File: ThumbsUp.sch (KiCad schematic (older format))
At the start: 169 parts, among them IC1 RP2040, IC2 W25Q128JVSIM, IC3 RP2040, IC4 W25Q128JVSIM, J1 Conn_01x04_Male, J10 Raiser_Male, J11 Raiser_Female, J12 Raiser_Male, J13 Raiser_Female, J14 Raiser_Male, J15 Raiser_Female, J16 Raiser_Male, J17 Raiser_Female, J18 Raiser_Male, J19 Raiser_Female, J2 Conn_01x04_Male, J20 Conn_01x04_Female, J21 Conn_01x04_Female, J22 Conn_01x04_Female, J23 Conn_01x04_Female, J24 Conn_01x04_Male, J25 Conn_01x04_Male, J26 Conn_01x04_Male, J27 Conn_01x04_Male, J28 Conn_01x04_Female, J29 Conn_01x04_Female, J3 Conn_01x04_Female, J30 Conn_01x04_Female, J31 Conn_01x04_Female, J32 USB_C_Receptacle_USB2.0, J33 Raiser_Male, J34 Raiser_Female, J35 Raiser_Male, J36 STX-3501-3N, J37 USB_C_Receptacle_USB2.0, J38 Raiser_Female, J39 Raiser_Male, J4 Conn_01x04_Male, J40 Raiser_Female, J41 Raiser_Male, J42 Raiser_Female, J43 Raiser_Male, J44 Raiser_Female, J45 Raiser_Male, J46 STX-3501-3N, J47 Raiser_Female, J48 Raiser_Male, J49 Raiser_Female, J5 Conn_01x04_Female, J50 Raiser_Male, J51 Raiser_Female, J52 Raiser_Male, J6 Conn_01x04_Male, J7 Conn_01x04_Male, J8 Conn_01x04_Male, J9 Raiser_Female, U1 NCP1117-3.3_SOT223, U2 NCP1117-3.3_SOT223, Y1 ABLS-12.000MHZ-B4-T, Y2 ABLS-12.000MHZ-B4-T

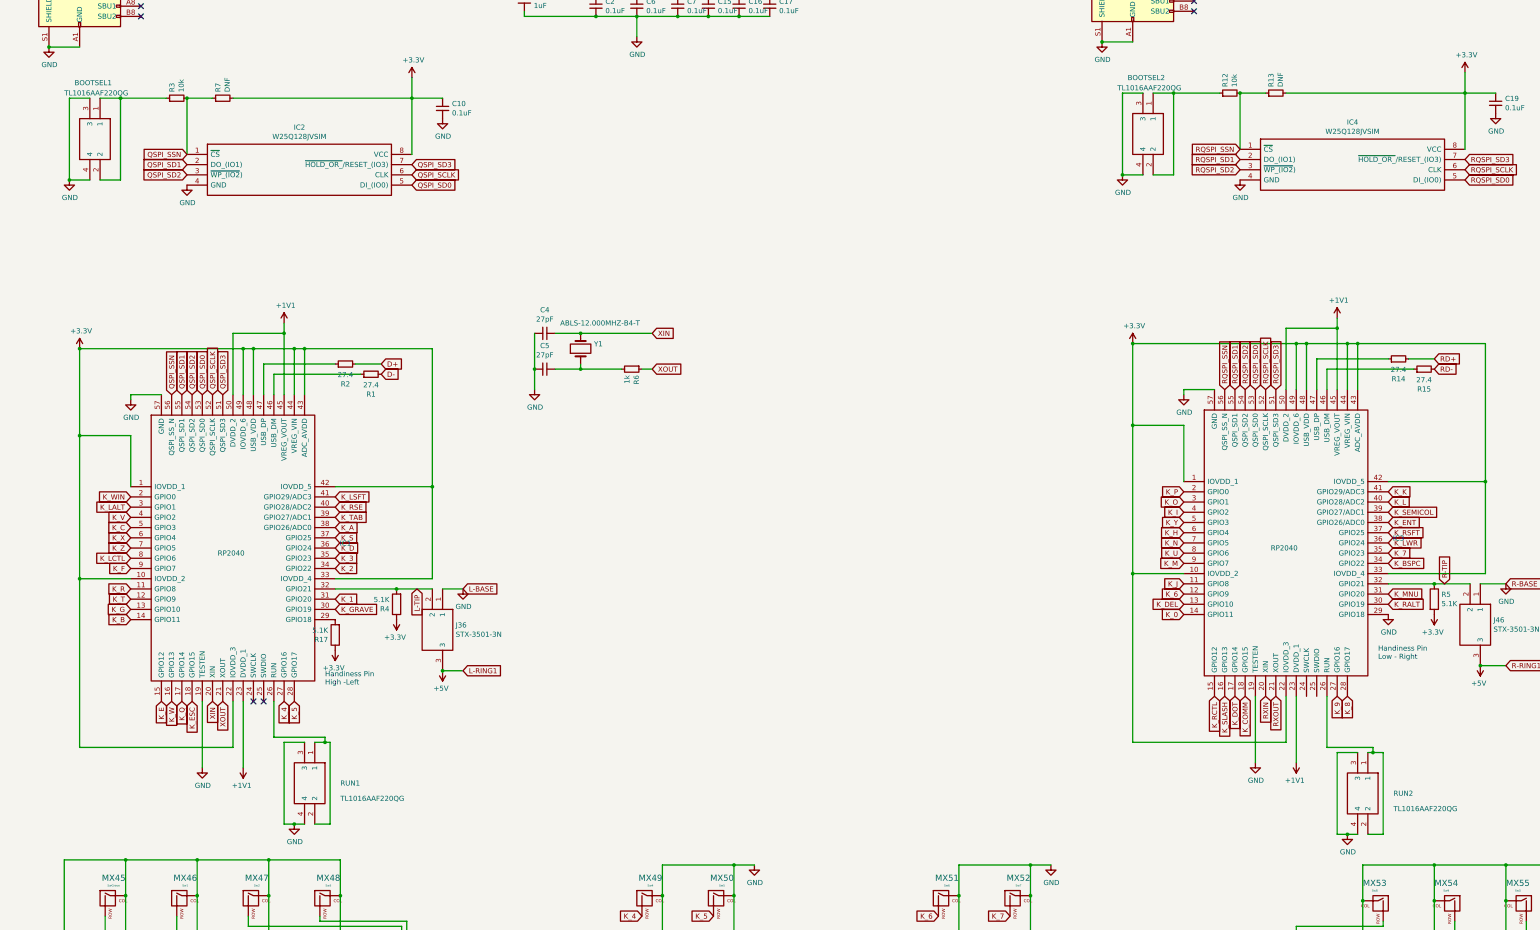
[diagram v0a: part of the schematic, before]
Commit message: Adjusted outlines, replaced pushbuttons
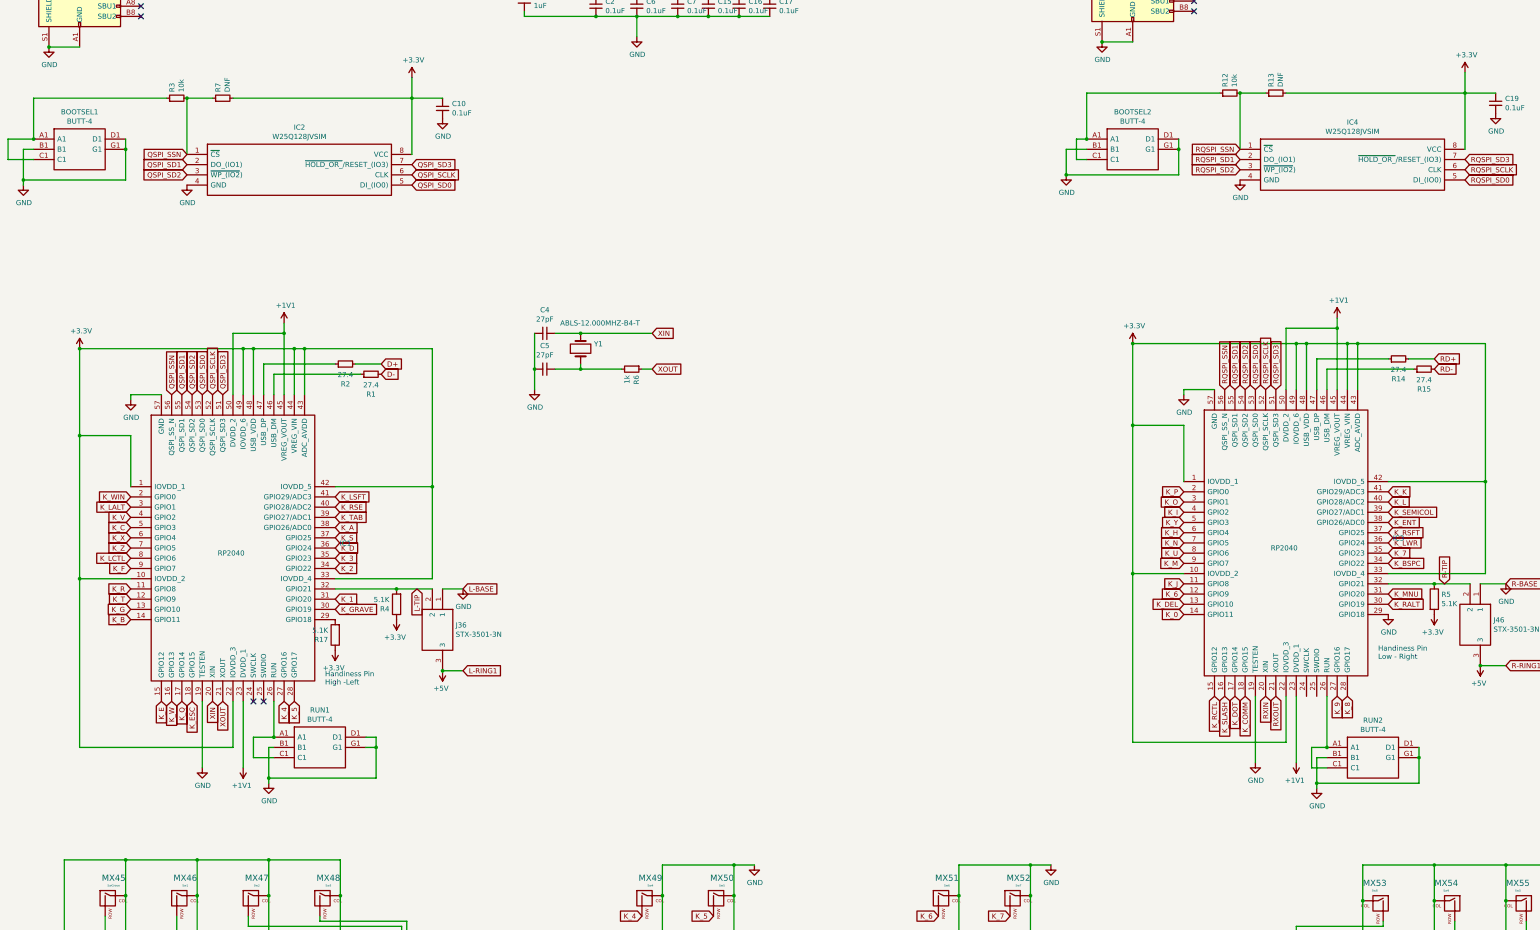
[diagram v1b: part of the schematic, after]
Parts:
- removed BOOTSEL1, BOOTSEL2, RUN1, RUN2: TL1016AAF220QG, TL1016AAF220QG:TL1016AAF220QG, symbol TL1016AAF220QG:TL1016AAF220QG
- added BOOTSEL1, BOOTSEL2, RUN1, RUN2: BUTT-4, BUTT4, symbol BUTT-4:BUTT-4
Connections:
- net GND: now also BOOTSEL1.B1, BOOTSEL1.D1, BOOTSEL1.G1, BOOTSEL2.B1, BOOTSEL2.D1, BOOTSEL2.G1, RUN1.B1, RUN1.D1, RUN1.G1, RUN2.B1, RUN2.D1, RUN2.G1
- net at R3.1: now also BOOTSEL1.A1, BOOTSEL1.C1
- net at IC1.26 (RUN): now also RUN1.A1, RUN1.C1
- net at R12.1: now also BOOTSEL2.A1, BOOTSEL2.C1
- net at IC3.26 (RUN): now also RUN2.A1, RUN2.C1

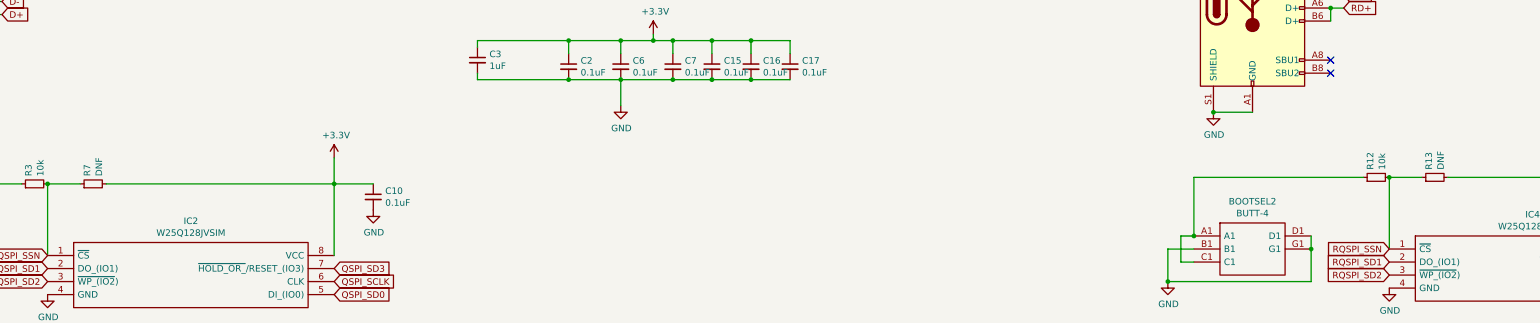
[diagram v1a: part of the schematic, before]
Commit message: Populated DNF resistors with 10K.
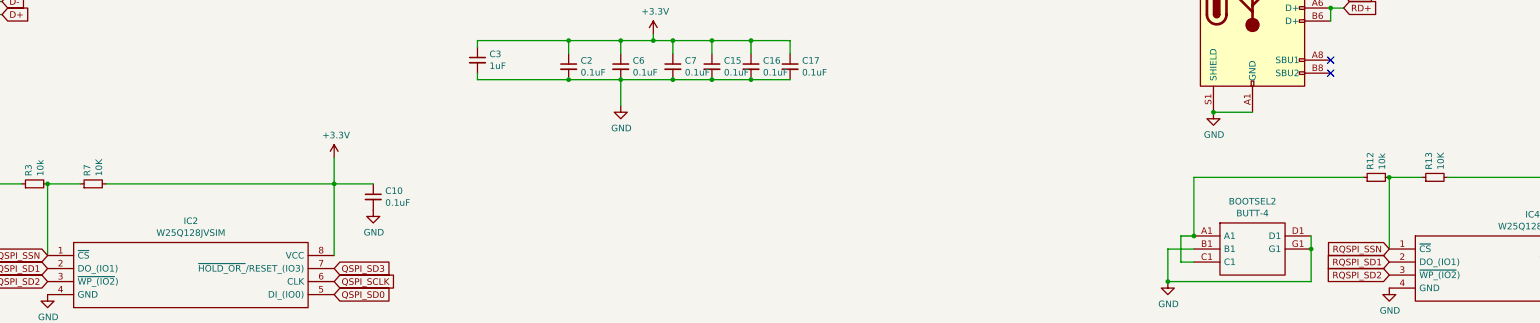
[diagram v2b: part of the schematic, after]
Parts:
- BOOTSEL1, BOOTSEL2, RUN1, RUN2: footprint BUTT4 -> KiCad:BUTT4
- R13, R7: value DNF -> 10K
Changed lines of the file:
@@
 P 3150 3300
 F 0 "R7" H 3209 3346 50  0000 L CNN
-F 1 "DNF" H 3209 3255 50  0000 L CNN
+F 1 "10K" H 3209 3255 50  0000 L CNN
 F 2 "Resistor_SMD:R_0402_1005Metric" H 3150 3300 50  0001 C CNN
 F 3 "~" H 3150 3300 50  0001 C CNN
@@
 P 13450 3250
 F 0 "R13" H 13509 3296 50  0000 L CNN
-F 1 "DNF" H 13509 3205 50  0000 L CNN
+F 1 "10K" H 13509 3205 50  0000 L CNN
 F 2 "Resistor_SMD:R_0402_1005Metric" H 13450 3250 50  0001 C CNN
 F 3 "~" H 13450 3250 50  0001 C CNN
@@
 F 0 "BOOTSEL1" H 1750 3965 50  0000 C CNN
 F 1 "BUTT-4" H 1750 3874 50  0000 C CNN
-F 2 "BUTT4" H 2050 3800 50  0001 L CNN
+F 2 "KiCad:BUTT4" H 2050 3800 50  0001 L CNN
 F 3 "http://site.gravitech.us/Components/BUTT-4/BUTT-4_datasheet.pdf" H 2050 3700 50  0001 L CNN
 F 4 "Tactile Switches MINI PUSH BUTTON SWITCH 4-PIN QTY. 4" H 2050 3600 50  0001 L CNN "Description"
@@
 F 0 "BOOTSEL2" H 12050 3965 50  0000 C CNN
 F 1 "BUTT-4" H 12050 3874 50  0000 C CNN
-F 2 "BUTT4" H 12350 3800 50  0001 L CNN
+F 2 "KiCad:BUTT4" H 12350 3800 50  0001 L CNN
 F 3 "http://site.gravitech.us/Components/BUTT-4/BUTT-4_datasheet.pdf" H 12350 3700 50  0001 L CNN
 F 4 "Tactile Switches MINI PUSH BUTTON SWITCH 4-PIN QTY. 4" H 12350 3600 50  0001 L CNN "Description"
@@
 F 0 "RUN2" H 14400 9915 50  0000 C CNN
 F 1 "BUTT-4" H 14400 9824 50  0000 C CNN
-F 2 "BUTT4" H 14700 9750 50  0001 L CNN
+F 2 "KiCad:BUTT4" H 14700 9750 50  0001 L CNN
 F 3 "http://site.gravitech.us/Components/BUTT-4/BUTT-4_datasheet.pdf" H 14700 9650 50  0001 L CNN
 F 4 "Tactile Switches MINI PUSH BUTTON SWITCH 4-PIN QTY. 4" H 14700 9550 50  0001 L CNN "Description"
@@
 F 0 "RUN1" H 4100 9815 50  0000 C CNN
 F 1 "BUTT-4" H 4100 9724 50  0000 C CNN
-F 2 "BUTT4" H 4400 9650 50  0001 L CNN
+F 2 "KiCad:BUTT4" H 4400 9650 50  0001 L CNN
 F 3 "http://site.gravitech.us/Components/BUTT-4/BUTT-4_datasheet.pdf" H 4400 9550 50  0001 L CNN
 F 4 "Tactile Switches MINI PUSH BUTTON SWITCH 4-PIN QTY. 4" H 4400 9450 50  0001 L CNN "Description"

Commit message: Replacing voltage regulators with available parts - PCBs updated.
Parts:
- C11, C18: value 10uF -> 100uF; footprint Capacitor_SMD:C_0402_1005Metric -> Capacitor_SMD:C_1210_3225Metric; symbol Device:C_Small -> TAJB107K006RNJV:TAJB107K006RNJV
- U1, U2: value NCP1117-3.3_SOT223 -> AMS1117-3.3_SOT223; footprint Package_TO_SOT_SMD:SOT-223-3_TabPin2 -> AMS1117-3.3:SOT229P700X180-4N
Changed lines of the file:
@@
 P 4850 1250
 F 0 "U1" H 4850 1492 50  0000 C CNN
-F 1 "NCP1117-3.3_SOT223" H 4850 1401 50  0000 C CNN
-F 2 "Package_TO_SOT_SMD:SOT-223-3_TabPin2" H 4850 1450 50  0001 C CNN
+F 1 "AMS1117-3.3_SOT223" H 4850 1401 50  0000 C CNN
+F 2 "AMS1117-3.3:SOT229P700X180-4N" H 4850 1450 50  0001 C CNN
 F 3 "http://www.onsemi.com/pub_link/Collateral/NCP1117-D.PDF" H 4950 1000 50  0001 C CNN
 	1    4850 1250
@@
 $EndComp
 $Comp
-L Device:C_Small C11
+L TAJB107K006RNJV:TAJB107K006RNJV C11
 U 1 1 6390456E
-P 5250 1350
-F 0 "C11" H 5342 1396 50  0000 L CNN
-F 1 "10uF" H 5342 1305 50  0000 L CNN
-F 2 "Capacitor_SMD:C_0402_1005Metric" H 5250 1350 50  0001 C CNN
-F 3 "~" H 5250 1350 50  0001 C CNN
-	1    5250 1350
-	1    0    0    -1
+P 5250 1250
+F 0 "C11" V 5450 1400 50  0000 L CNN
+F 1 "100uF" V 5550 1400 50  0000 L CNN
+F 2 "Capacitor_SMD:C_1210_3225Metric" H 5250 1250 50  0001 C CNN
+F 3 "~" H 5250 1250 50  0001 C CNN
+	1    5250 1250
+	0    1    1    0
 $EndComp
 $Comp
 L power:GND #PWR0102
 U 1 1 63904A46
-P 5250 1450
-F 0 "#PWR0102" H 5250 1200 50  0001 C CNN
-F 1 "GND" H 5255 1277 50  0000 C CNN
-F 2 "" H 5250 1450 50  0001 C CNN
-F 3 "" H 5250 1450 50  0001 C CNN
-	1    5250 1450
+P 5250 1750
+F 0 "#PWR0102" H 5250 1500 50  0001 C CNN
+F 1 "GND" H 5255 1577 50  0000 C CNN
+F 2 "" H 5250 1750 50  0001 C CNN
+F 3 "" H 5250 1750 50  0001 C CNN
+	1    5250 1750
 	1    0    0    -1
 $EndComp
@@
 	1    0    0    -1
 $EndComp
-Wire Wire Line
-	5150 1250 5250 1250
-Connection ~ 5250 1250
-Wire Wire Line
-	5250 1250 5550 1250
 $Comp
 L power:+3.3V #PWR0105
@@
 P 15150 1200
 F 0 "U2" H 15150 1442 50  0000 C CNN
-F 1 "NCP1117-3.3_SOT223" H 15150 1351 50  0000 C CNN
-F 2 "Package_TO_SOT_SMD:SOT-223-3_TabPin2" H 15150 1400 50  0001 C CNN
+F 1 "AMS1117-3.3_SOT223" H 15150 1351 50  0000 C CNN
+F 2 "AMS1117-3.3:SOT229P700X180-4N" H 15150 1400 50  0001 C CNN
 F 3 "http://www.onsemi.com/pub_link/Collateral/NCP1117-D.PDF" H 15250 950 50  0001 C CNN
 	1    15150 1200
@@
 $EndComp
 $Comp
-L Device:C_Small C18
+L TAJB107K006RNJV:TAJB107K006RNJV C18
 U 1 1 63C337FB
-P 15550 1300
-F 0 "C18" H 15642 1346 50  0000 L CNN
-F 1 "10uF" H 15642 1255 50  0000 L CNN
-F 2 "Capacitor_SMD:C_0402_1005Metric" H 15550 1300 50  0001 C CNN
-F 3 "~" H 15550 1300 50  0001 C CNN
-	1    15550 1300
-	1    0    0    -1
+P 15550 1200
+F 0 "C18" V 15700 1400 50  0000 L CNN
+F 1 "100uF" V 15800 1400 50  0000 L CNN
+F 2 "Capacitor_SMD:C_1210_3225Metric" H 15550 1200 50  0001 C CNN
+F 3 "~" H 15550 1200 50  0001 C CNN
+	1    15550 1200
+	0    1    1    0
 $EndComp
 $Comp
 L power:GND #PWR0131
 U 1 1 63C33801
-P 15550 1400
-F 0 "#PWR0131" H 15550 1150 50  0001 C CNN
-F 1 "GND" H 15555 1227 50  0000 C CNN
-F 2 "" H 15550 1400 50  0001 C CNN
-F 3 "" H 15550 1400 50  0001 C CNN
-	1    15550 1400
+P 15550 1700
+F 0 "#PWR0131" H 15550 1450 50  0001 C CNN
+F 1 "GND" H 15555 1527 50  0000 C CNN
+F 2 "" H 15550 1700 50  0001 C CNN
+F 3 "" H 15550 1700 50  0001 C CNN
+	1    15550 1700
 	1    0    0    -1
 $EndComp
@@
 	1    0    0    -1
 $EndComp
-Wire Wire Line
-	15450 1200 15550 1200
-Connection ~ 15550 1200
-Wire Wire Line
-	15550 1200 15850 1200
 $Comp
 L power:+3.3V #PWR0133
@@
 Wire Wire Line
 	13850 10000 13850 10050
+Wire Wire Line
+	5150 1250 5250 1250
+Connection ~ 5250 1250
+Wire Wire Line
+	5250 1250 5550 1250
+Wire Wire Line
+	15450 1200 15550 1200
+Connection ~ 15550 1200
+Wire Wire Line
+	15550 1200 15850 1200
 $EndSCHEMATC
